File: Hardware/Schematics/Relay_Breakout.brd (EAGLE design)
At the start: 31 x 36 mm, 17 parts, among them J1 1X2-3.5MM, J2 1X2-3.5MM

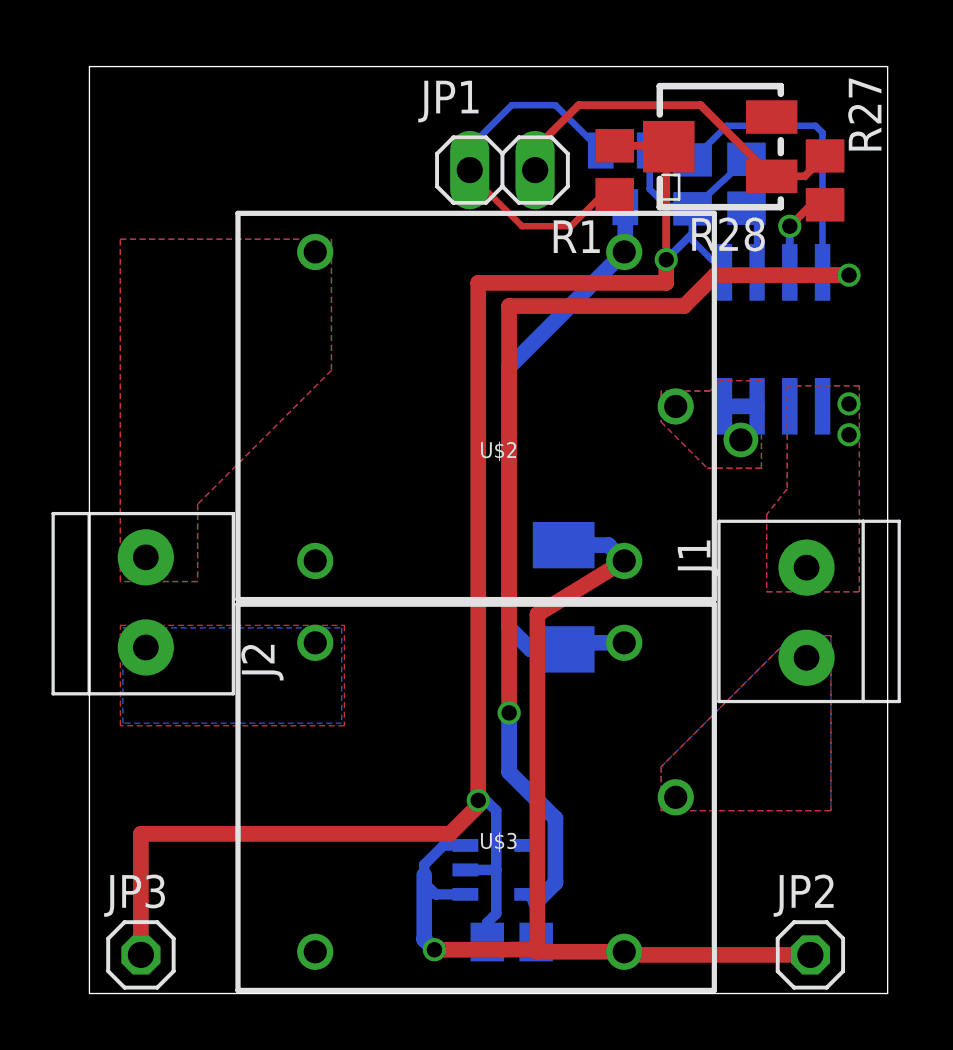
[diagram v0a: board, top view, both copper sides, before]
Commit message: Started implementing handling of button event. Code is not yet tested.
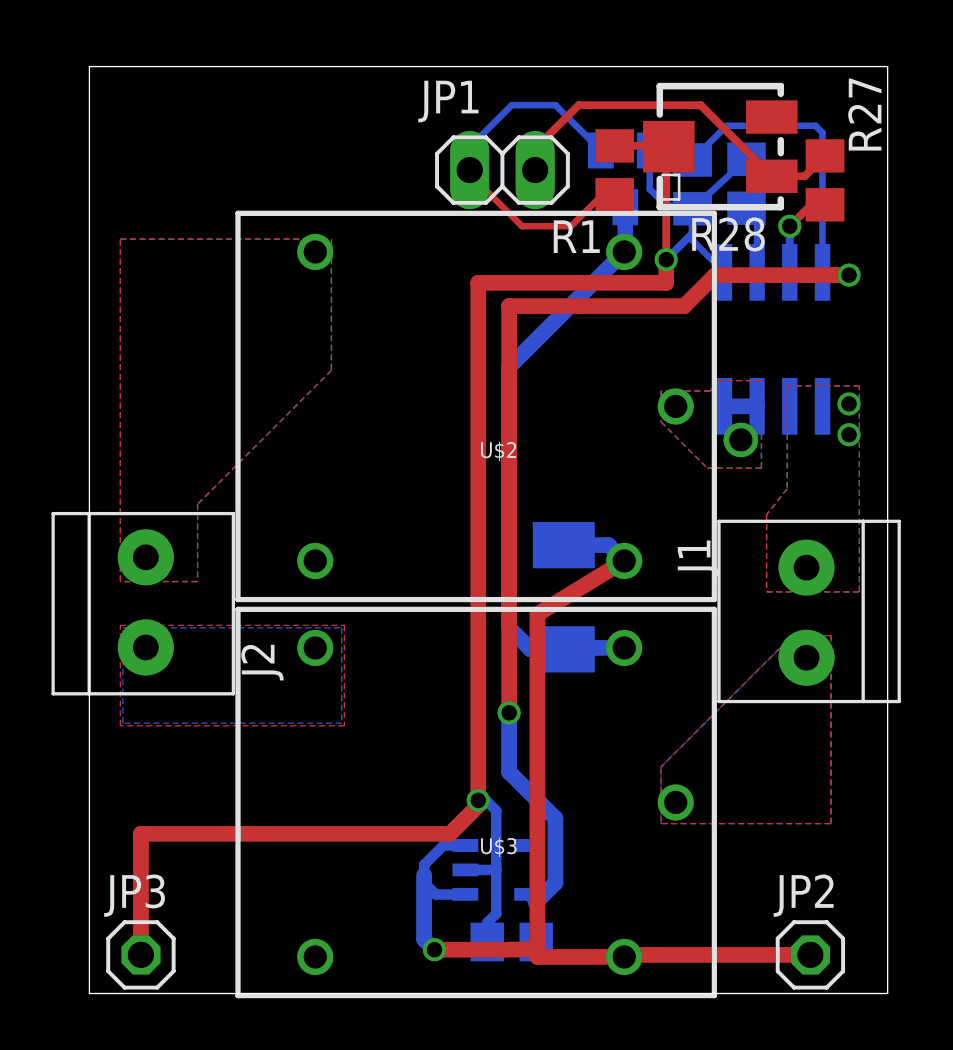
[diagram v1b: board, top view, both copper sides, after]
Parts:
- moved U$3 0.20 mm to (15.4, 7.30)
